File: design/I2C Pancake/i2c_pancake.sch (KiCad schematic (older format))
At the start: 24 parts, among them J1 Conn_01x03, J2 Conn_01x03, P1 CONN_01X02, Q1 2N3096, U1 TL780-15, U2 LT1460-10

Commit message: Add MCU and finish schematic
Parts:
- removed C2: 330 nF, Capacitors_SMD:C_0805_HandSoldering, symbol i2c_pancake-rescue:C-device
- removed C3: 220 nF, Capacitors_SMD:C_0805_HandSoldering, symbol i2c_pancake-rescue:C-device
- removed R2: 20K, Resistors_SMD:R_0805_HandSoldering, symbol i2c_pancake-rescue:R-device
- removed R4: 10K, Resistors_SMD:R_0805_HandSoldering, symbol i2c_pancake-rescue:R-device
- removed U1: TL780-15, TO_SOT_Packages_THT:TO-220-3_Vertical, symbol i2c_pancake-rescue:TL780-15-daq_components
- added C8: 22uF, symbol Device:C
- added D1: D, symbol Device:D
- added R15: 10K, symbol Device:R
- added R17: R, symbol Device:R
- added U6: PIC16F1826-ISO, symbol rlcsv3_modular-rescue:PIC16F1826-ISO
- R12, R13, R14, R16: renamed from R?; value R -> 10K
- gave numbers to parts that had none: 4
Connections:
- net labels removed: +15V, +16V
- wire segments 111 -> 103
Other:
- note removed: "voltage monitoring (optional)"
- moved on the sheet: C1, C4, F1, J1, J2, J3, J7, J8, P1, Q1, R1, R12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

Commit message: Fix some suggestions
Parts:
- removed D1: D, symbol Device:D
- added D1: LED, symbol Device:LED
- R17: value R -> 10K; footprint (none) -> Resistor_SMD:R_0805_2012Metric_Pad1.15x1.40mm_HandSolder
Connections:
- net at U6.14 (VDD): now also D1.2 (A)
- net at R17.1: now also D1.1 (K)
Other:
- moved on the sheet: C8
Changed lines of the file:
@@
 $Descr A4 11693 8268
 encoding utf-8
-Sheet 1 3
+Sheet 1 4
 Title ""
 Date ""
@@
 L power:GND #PWR046
 U 1 1 5E6EB0CC
-P 7000 1050
-F 0 "#PWR046" H 7000 800 50  0001 C CNN
-F 1 "GND" H 7005 877 50  0000 C CNN
-F 2 "" H 7000 1050 50  0001 C CNN
-F 3 "" H 7000 1050 50  0001 C CNN
-	1    7000 1050
+P 7000 700
+F 0 "#PWR046" H 7000 450 50  0001 C CNN
+F 1 "GND" H 7005 527 50  0000 C CNN
+F 2 "" H 7000 700 50  0001 C CNN
+F 3 "" H 7000 700 50  0001 C CNN
+	1    7000 700
 	1    0    0    -1
 $EndComp
@@
 L power:+12V #PWR043
 U 1 1 5E6EBD9D
-P 6500 1050
-F 0 "#PWR043" H 6500 900 50  0001 C CNN
-F 1 "+12V" H 6515 1223 50  0000 C CNN
-F 2 "" H 6500 1050 50  0001 C CNN
-F 3 "" H 6500 1050 50  0001 C CNN
-	1    6500 1050
+P 6500 700
+F 0 "#PWR043" H 6500 550 50  0001 C CNN
+F 1 "+12V" H 6515 873 50  0000 C CNN
+F 2 "" H 6500 700 50  0001 C CNN
+F 3 "" H 6500 700 50  0001 C CNN
+	1    6500 700
 	1    0    0    -1
 $EndComp
@@
 L power:+5V #PWR045
 U 1 1 5E6ECC01
-P 6700 1050
-F 0 "#PWR045" H 6700 900 50  0001 C CNN
-F 1 "+5V" H 6715 1223 50  0000 C CNN
-F 2 "" H 6700 1050 50  0001 C CNN
-F 3 "" H 6700 1050 50  0001 C CNN
-	1    6700 1050
+P 6700 700
+F 0 "#PWR045" H 6700 550 50  0001 C CNN
+F 1 "+5V" H 6715 873 50  0000 C CNN
+F 2 "" H 6700 700 50  0001 C CNN
+F 3 "" H 6700 700 50  0001 C CNN
+	1    6700 700
 	1    0    0    -1
 $EndComp
 Connection ~ 6700 1650
 Connection ~ 6500 1750
-Connection ~ 6900 1550
-Wire Wire Line
-	6900 950  7000 950
-Wire Wire Line
-	7000 950  7000 1050
-Wire Wire Line
-	6900 950  6900 1550
-Wire Wire Line
-	6500 1050 6500 1750
-Wire Wire Line
-	6700 1050 6700 1650
 Wire Wire Line
 	6100 1850 7200 1850
@@
 L power:+5V #PWR042
 U 1 1 5E756FED
-P 7600 3450
-F 0 "#PWR042" H 7600 3300 50  0001 C CNN
-F 1 "+5V" H 7615 3623 50  0000 C CNN
-F 2 "" H 7600 3450 50  0001 C CNN
-F 3 "" H 7600 3450 50  0001 C CNN
-	1    7600 3450
+P 7050 3650
+F 0 "#PWR042" H 7050 3500 50  0001 C CNN
+F 1 "+5V" H 7065 3823 50  0000 C CNN
+F 2 "" H 7050 3650 50  0001 C CNN
+F 3 "" H 7050 3650 50  0001 C CNN
+	1    7050 3650
 	1    0    0    -1
 $EndComp
@@
 L power:GND #PWR044
 U 1 1 5E757BCE
-P 8050 3700
-F 0 "#PWR044" H 8050 3450 50  0001 C CNN
-F 1 "GND" H 8055 3527 50  0000 C CNN
-F 2 "" H 8050 3700 50  0001 C CNN
-F 3 "" H 8050 3700 50  0001 C CNN
-	1    8050 3700
+P 7550 3950
+F 0 "#PWR044" H 7550 3700 50  0001 C CNN
+F 1 "GND" H 7555 3777 50  0000 C CNN
+F 2 "" H 7550 3950 50  0001 C CNN
+F 3 "" H 7550 3950 50  0001 C CNN
+	1    7550 3950
 	1    0    0    -1
 $EndComp
@@
 P 6850 5000
 F 0 "R17" H 6920 5046 50  0000 L CNN
-F 1 "R" H 6920 4955 50  0000 L CNN
-F 2 "" V 6780 5000 50  0001 C CNN
+F 1 "10K" H 6920 4955 50  0000 L CNN
+F 2 "Resistor_SMD:R_0805_2012Metric_Pad1.15x1.40mm_HandSolder" V 6780 5000 50  0001 C CNN
 F 3 "~" H 6850 5000 50  0001 C CNN
 	1    6850 5000
@@
 	4900 3900 5350 3900
 Wire Wire Line
-	7050 3650 7600 3650
-Wire Wire Line
-	7600 3650 7600 3450
-Connection ~ 7600 3650
-Wire Wire Line
-	7600 3650 7650 3650
-Wire Wire Line
-	7950 3650 8050 3650
-$Comp
-L Device:D D1
-U 1 1 5E76F58B
-P 6850 4600
-F 0 "D1" V 6896 4521 50  0000 R CNN
-F 1 "D" V 6805 4521 50  0000 R CNN
-F 2 "" H 6850 4600 50  0001 C CNN
-F 3 "~" H 6850 4600 50  0001 C CNN
-	1    6850 4600
-	0    -1   -1   0
-$EndComp
-Wire Wire Line
 	6350 4350 6850 4350
 Wire Wire Line
-	6850 4350 6850 4450
-Wire Wire Line
 	6850 4750 6850 4850
-Wire Wire Line
-	8050 3700 8050 3650
 Wire Wire Line
 	6850 5200 6850 5150
@@
 L Device:C C8
 U 1 1 5E76575E
-P 7800 3650
-F 0 "C8" V 7548 3650 50  0000 C CNN
-F 1 "22uF" V 7639 3650 50  0000 C CNN
-F 2 "" H 7838 3500 50  0001 C CNN
-F 3 "~" H 7800 3650 50  0001 C CNN
-	1    7800 3650
+P 7300 3900
+F 0 "C8" V 7048 3900 50  0000 C CNN
+F 1 "22uF" V 7139 3900 50  0000 C CNN
+F 2 "" H 7338 3750 50  0001 C CNN
+F 3 "~" H 7300 3900 50  0001 C CNN
+	1    7300 3900
 	0    1    1    0
 $EndComp
-Wire Wire Line
-	7050 3900 7050 3650
 Wire Wire Line
 	6350 3900 7050 3900
@@
 Connection ~ 8150 5800
 $Comp
-L power:+10V #PWR?
+L power:+10V #PWR05
 U 1 1 5E81B1CC
 P 9600 1100
-F 0 "#PWR?" H 9600 950 50  0001 C CNN
+F 0 "#PWR05" H 9600 950 50  0001 C CNN
 F 1 "+10V" H 9615 1273 50  0000 C CNN
 F 2 "" H 9600 1100 50  0001 C CNN
@@
 $EndComp
 $Comp
-L power:+10V #PWR?
+L power:+10V #PWR06
 U 1 1 5E81B838
 P 9600 1950
-F 0 "#PWR?" H 9600 1800 50  0001 C CNN
+F 0 "#PWR06" H 9600 1800 50  0001 C CNN
 F 1 "+10V" H 9615 2123 50  0000 C CNN
 F 2 "" H 9600 1950 50  0001 C CNN
@@
 Wire Wire Line
 	4250 3750 5350 3750
+$Comp
+L Device:LED D1
+U 1 1 5E6C4A64
+P 6850 4600
+F 0 "D1" V 6889 4483 50  0000 R CNN
+F 1 "LED" V 6798 4483 50  0000 R CNN
+F 2 "" H 6850 4600 50  0001 C CNN
+F 3 "~" H 6850 4600 50  0001 C CNN
+	1    6850 4600
+	0    -1   -1   0
+$EndComp
+Wire Wire Line
+	6850 4350 6850 4450
+Wire Wire Line
+	7050 3650 7050 3900
+Wire Wire Line
+	7050 3900 7150 3900
+Connection ~ 7050 3900
+Wire Wire Line
+	7450 3900 7550 3900
+Wire Wire Line
+	7550 3900 7550 3950
+Wire Wire Line
+	6700 700  6700 1650
+Wire Wire Line
+	6500 700  6500 1750
+Wire Wire Line
+	6900 1550 6900 600
+Wire Wire Line
+	6900 600  7000 600
+Wire Wire Line
+	7000 600  7000 700
+Connection ~ 6900 1550
 $EndSCHEMATC

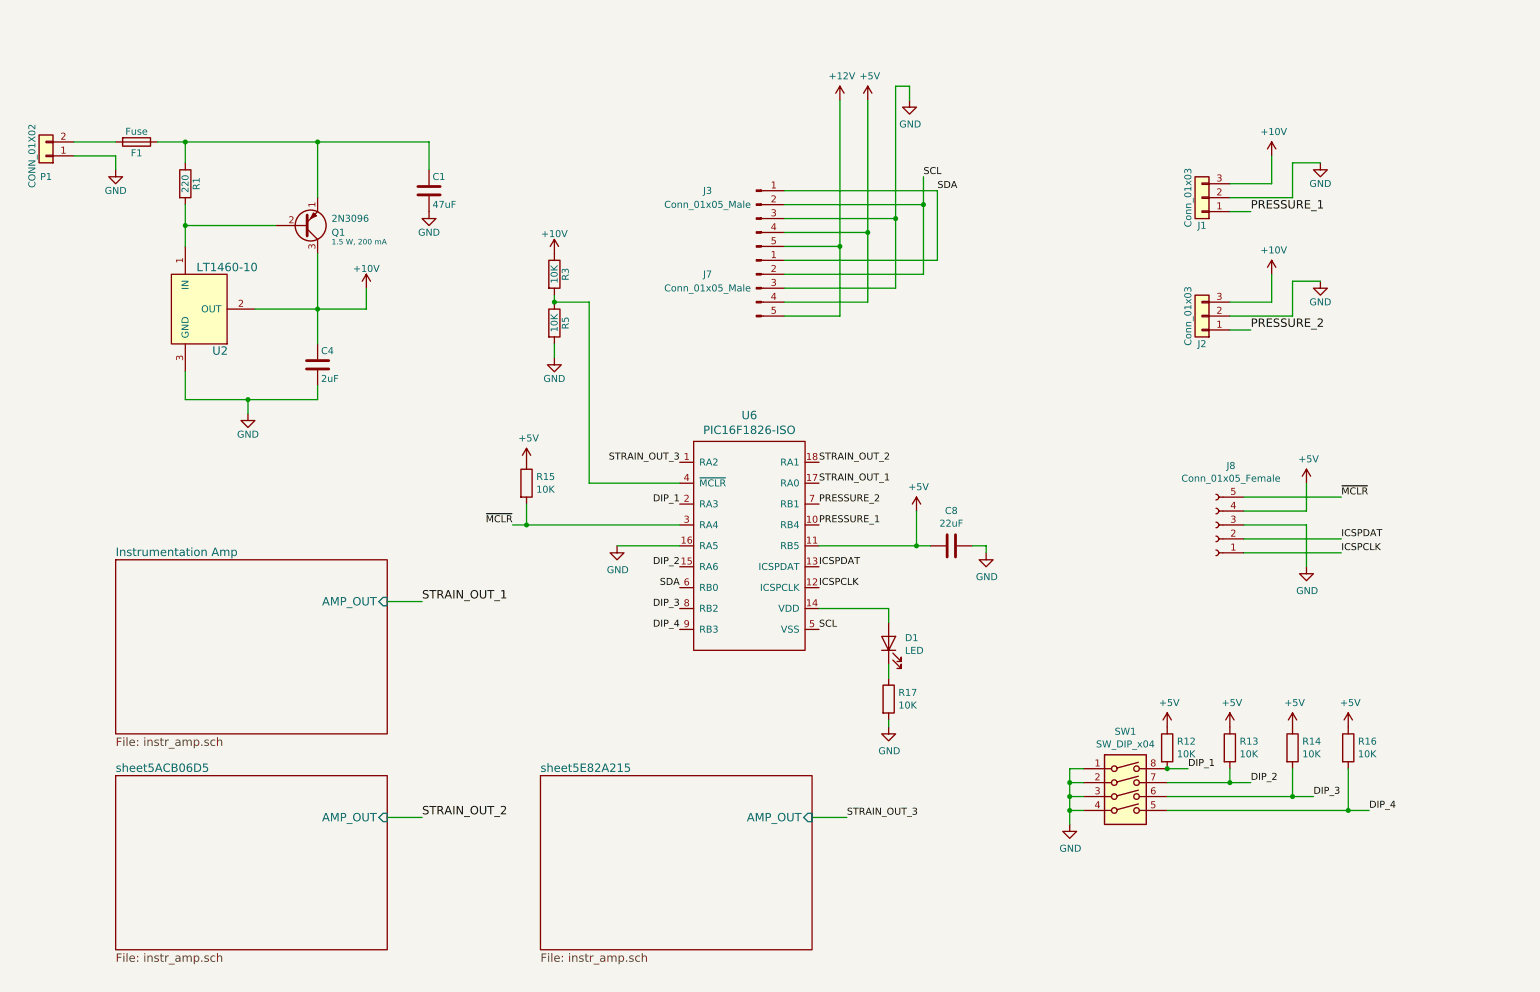
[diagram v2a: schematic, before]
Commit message: Finish adressing Alex and Jared's comments with the exception of issue with high drop out voltage on current amp.
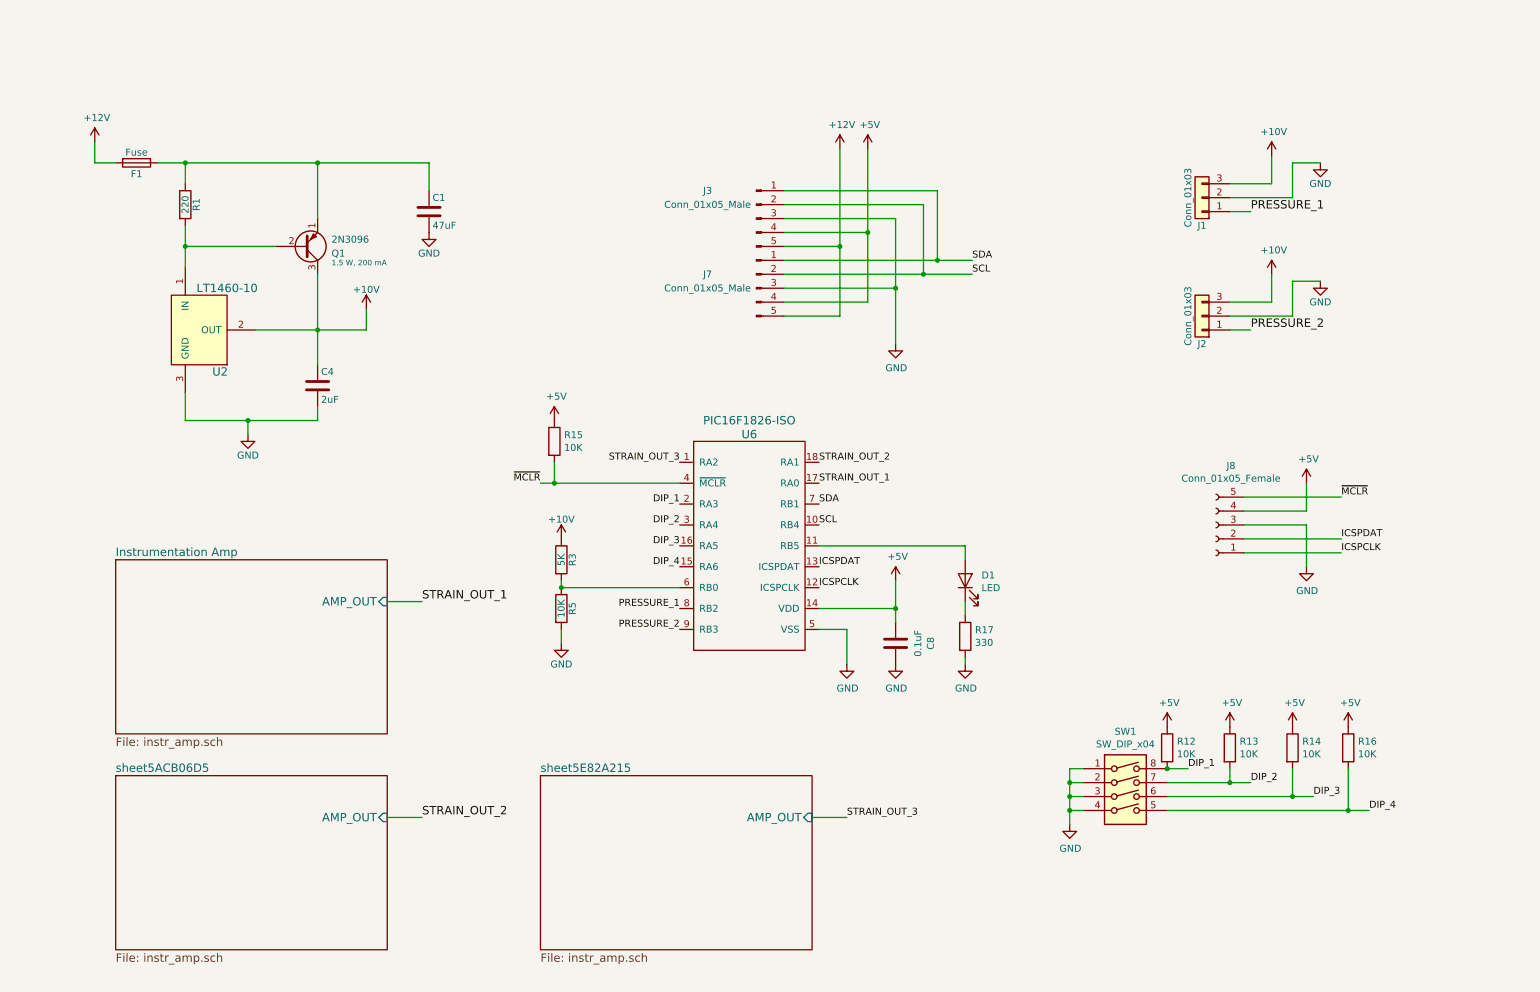
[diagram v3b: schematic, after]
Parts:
- removed P1: CONN_01X02, Connectors_Phoenix:PhoenixContact_MCV-G_02x3.50mm_Vertical, symbol i2c_pancake-rescue:Conn_01x02-strain_gauges_rtr-rescue
- C8: value 22uF -> 0.1uF
- R17: value 10K -> 330
- R3: value 10K -> 5K
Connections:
- net +12V: now also F1.2
- net +5V: now also U6.14 (VDD); no longer U6.11 (RB5)
- net DIP_2: now also U6.3 (RA4); no longer U6.15 (RA6)
- net DIP_3: now also U6.16 (RA5); no longer U6.8 (RB2)
- net DIP_4: now also U6.15 (RA6); no longer U6.9 (RB3)
- net GND: now also U6.5 (VSS); no longer U6.16 (RA5)
- net PRESSURE_1: now also U6.8 (RB2); no longer U6.10 (RB4)
- net PRESSURE_2: now also U6.9 (RB3); no longer U6.7 (RB1)
- net SCL: now also U6.10 (RB4); no longer U6.5 (VSS)
- net SDA: now also U6.7 (RB1); no longer U6.6 (RB0)
- net ~MCLR: now also U6.4 (~MCLR); no longer U6.3 (RA4)
- net at R3.2, R5.1: now also U6.6 (RB0); no longer U6.4 (~MCLR)
- net at D1.2 (A): now also U6.11 (RB5); no longer U6.14 (VDD)
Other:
- moved on the sheet: C1, C4, C8, D1, F1, Q1, R1, R15, R17, R3, R5, U2
